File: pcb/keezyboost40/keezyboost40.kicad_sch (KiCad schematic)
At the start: 89 parts, among them SW1 SW_SPST, SW10 SW_SPST, SW11 SW_SPST, SW12 SW_SPST, SW13 SW_SPST, SW14 SW_SPST, SW15 SW_SPST, SW16 SW_SPST, SW17 SW_SPST, SW18 SW_SPST, SW19 SW_SPST, SW2 SW_SPST, SW20 SW_SPST, SW21 SW_SPST, SW22 SW_SPST, SW23 SW_SPST, SW24 SW_SPST, SW25 SW_SPST, SW26 SW_SPST, SW27 SW_SPST, SW28 SW_SPST, SW29 SW_SPST, SW3 SW_SPST, SW30 SW_SPST, SW31 SW_SPST, SW32 SW_SPST, SW33 SW_SPST, SW34 SW_SPST, SW35 SW_SPST, SW36 SW_SPST, SW37 SW_SPST, SW38 SW_SPST, SW39 SW_SPST, SW4 SW_SPST, SW40 SW_SPST, SW5 SW_SPST, SW6 SW_SPST, SW7 SW_SPST, SW8 SW_SPST, SW9 SW_SPST, U1 Pico, U2 ST7735_1.8inch

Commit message: finish v0.0
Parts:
- removed BZ1: Buzzer, symbol Device:Buzzer
- removed JP1: SolderJumper_2_Open, symbol Jumper:SolderJumper_2_Open
- removed JP2: (no value), symbol Jumper:SolderJumper_2_Open
- removed R1: R, symbol Device:R
- removed R2: (no value), symbol Device:R
- removed RV1: R_Potentiometer_Trim, symbol Device:R_Potentiometer_Trim
- removed RV2: (no value), symbol Device:R_Potentiometer_Trim
- added H1, H5: (no value), symbol Mechanical:MountingHole
- added H10, H2, H3, H4, H6, H7, H8, H9: MountingHole, symbol Mechanical:MountingHole
- U1: footprint RPi_Pico:RPi_Pico_SMD_TH -> (none)
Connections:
- net 3v3: now also U2.1 (VCC)

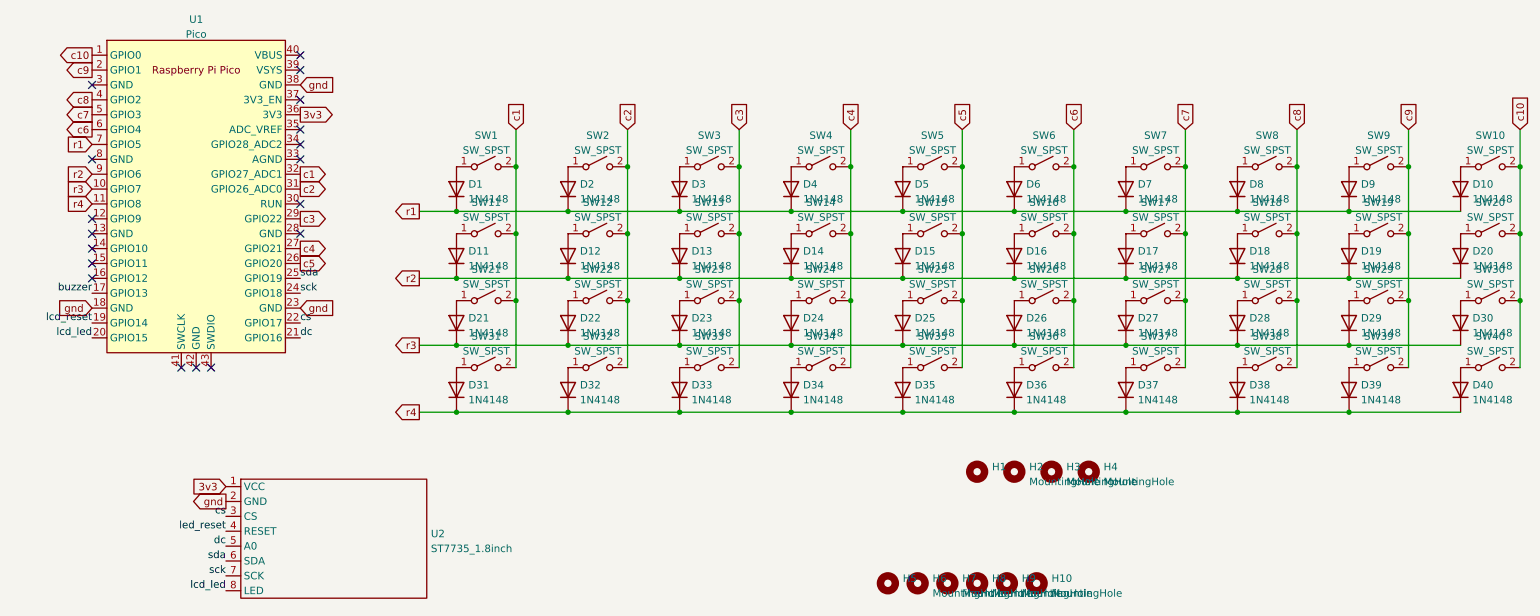
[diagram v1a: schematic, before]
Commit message: fixup issues with lcd interface connections
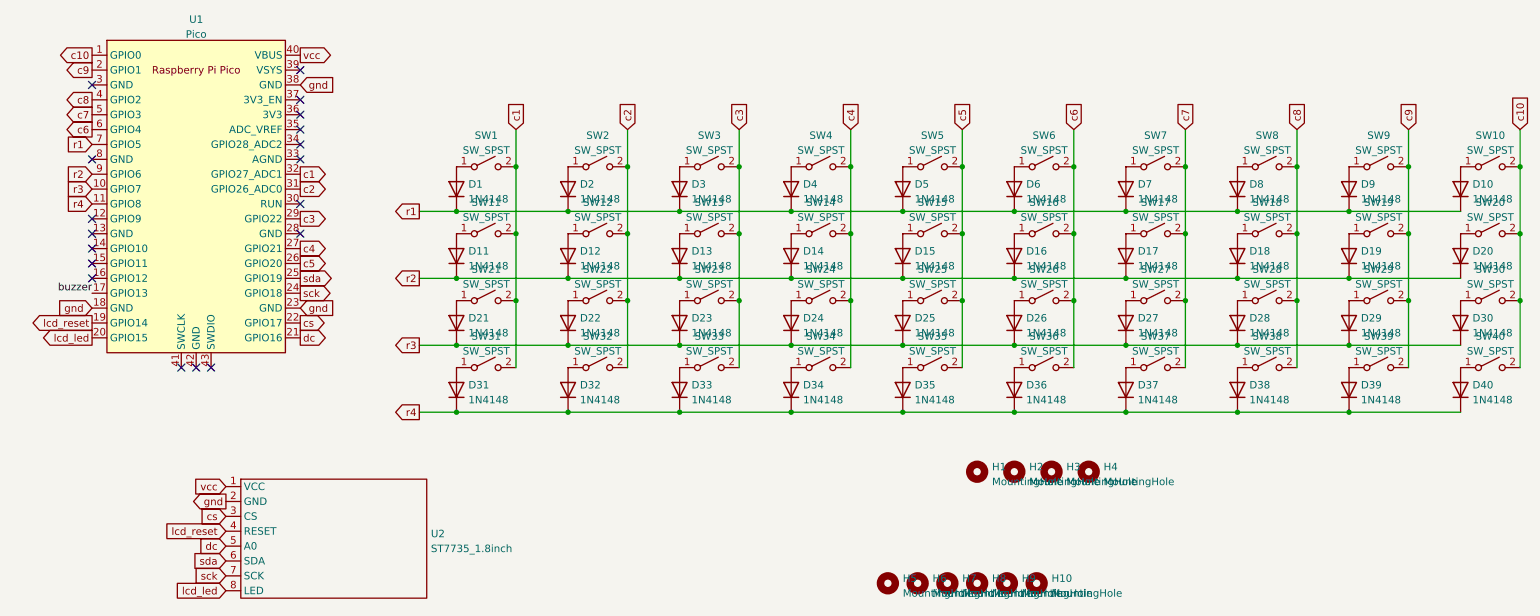
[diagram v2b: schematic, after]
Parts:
- D1, D10, D11, D12, D13, D14, D15, D16, D17, D18, D19, D2, D20, D21, D22, D23, D24, D25, D26, D27, D28, D29, D3, D30, D31, D32, D33, D34, D35, D36, D37, D38, D39, D4, D40, D5, D6, D7, D8, D9: footprint (none) -> Diode_SMD:D_SOD-123
- H1: value (none) -> MountingHole; footprint (none) -> MountingHole:MountingHole_2.2mm_M2_DIN965_Pad
- H10, H6, H7, H8, H9: footprint (none) -> MountingHole:MountingHole_2.2mm_M2
- H2, H3, H4: footprint (none) -> MountingHole:MountingHole_2.2mm_M2_DIN965_Pad
- H5: value (none) -> MountingHole; footprint (none) -> MountingHole:MountingHole_2.2mm_M2
- SW1, SW10, SW11, SW12, SW13, SW14, SW15, SW16, SW17, SW18, SW19, SW2, SW20, SW21, SW22, SW23, SW24, SW25, SW26, SW27, SW28, SW29, SW3, SW30, SW31, SW32, SW33, SW34, SW35, SW36, SW37, SW38, SW39, SW4, SW40, SW5, SW6, SW7, SW8, SW9: footprint (none) -> keyswitches:Kailh_socket_PG1350
- U1: footprint (none) -> kicub_keyboard_extras:RPi_Pico_SMD_TH_OPEN
- U2: footprint (none) -> kicub_keyboard_extras:ST7735_1.8inch
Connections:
- net led_reset is gone; now on net lcd_reset: U2.4 (RESET)
- net vcc: now reaches U1.40 (VBUS)
- net vcc: now also U2.1 (VCC)
- net 3v3: no longer names the net of U1.36 (3V3)
- net 3v3: no longer U2.1 (VCC)

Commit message: make lcd use 3.3v over 5v
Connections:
- net vcc: now also U1.36 (3V3); no longer U1.40 (VBUS)
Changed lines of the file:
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@@
   (no_connect (at 26.67 60.96))
   (no_connect (at 26.67 50.8))
+  (no_connect (at 62.23 33.02))
   (no_connect (at 62.23 40.64))
   (no_connect (at 62.23 35.56))
@@
   (no_connect (at 44.45 86.36))
   (no_connect (at 46.99 86.36))
-  (no_connect (at 62.23 43.18))
   (wire (pts (xy 137.16 74.93) (xy 137.16 86.36))
     (stroke (width 0) (type default) (color 0 0 0 0))
@@
     )
   )
+  (global_label "vcc" (shape output) (at 62.23 43.18 0) (fields_autoplaced)
+    (effects (font (size 1.27 1.27)) (justify left))
+    (property "Intersheet References" "${INTERSHEET_REFS}" (id 0) (at 67.7879 43.1006 0)
+      (effects (font (size 1.27 1.27)) (justify left) hide)
+    )
+  )
   (global_label "sck" (shape output) (at 62.23 73.66 0) (fields_autoplaced)
     (effects (font (size 1.27 1.27)) (justify left))
@@
     )
   )
-  (global_label "vcc" (shape output) (at 62.23 33.02 0) (fields_autoplaced)
-    (effects (font (size 1.27 1.27)) (justify left))
-    (property "Intersheet References" "${INTERSHEET_REFS}" (id 0) (at 67.7879 32.9406 0)
-      (effects (font (size 1.27 1.27)) (justify left) hide)
-    )
-  )

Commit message: add reset button
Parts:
- added SW41: (no value), symbol Switch:SW_SPST
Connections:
- net gnd: now also SW41.1 (A)
- net buzzer: no longer names the net of U1.17 (GPIO13)
- net buzzer: now also SW41.2 (B)
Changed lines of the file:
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@@
 (kicad_sch (version 20211123) (generator eeschema)
   (paper "A4")
+  (junction (at 21.59 76.2) (diameter 0) (color 0 0 0 0)
+  )
   (junction (at 222.25 93.98) (diameter 0) (color 0 0 0 0)
   )
@@
     (stroke (width 0) (type default) (color 0 0 0 0))
   )
+  (wire (pts (xy 20.32 76.2) (xy 21.59 76.2))
+    (stroke (width 0) (type default) (color 0 0 0 0))
+  )
   (wire (pts (xy 203.2 71.12) (xy 222.25 71.12))
     (stroke (width 0) (type default) (color 0 0 0 0))
@@
     (stroke (width 0) (type default) (color 0 0 0 0))
   )
+  (wire (pts (xy 21.59 73.66) (xy 21.59 76.2))
+    (stroke (width 0) (type default) (color 0 0 0 0))
+  )
   (wire (pts (xy 175.26 52.07) (xy 175.26 63.5))
     (stroke (width 0) (type default) (color 0 0 0 0))
@@
     (stroke (width 0) (type default) (color 0 0 0 0))
   )
+  (wire (pts (xy 16.51 73.66) (xy 21.59 73.66))
+    (stroke (width 0) (type default) (color 0 0 0 0))
+  )
   (wire (pts (xy 194.31 45.72) (xy 194.31 52.07))
     (stroke (width 0) (type default) (color 0 0 0 0))
@@
     (stroke (width 0) (type default) (color 0 0 0 0))
   )
+  (wire (pts (xy 21.59 76.2) (xy 26.67 76.2))
+    (stroke (width 0) (type default) (color 0 0 0 0))
+  )
   (wire (pts (xy 165.1 93.98) (xy 184.15 93.98))
     (stroke (width 0) (type default) (color 0 0 0 0))
@@
   (wire (pts (xy 156.21 63.5) (xy 156.21 74.93))
     (stroke (width 0) (type default) (color 0 0 0 0))
-  )
-  (label "buzzer" (at 26.67 73.66 180)
-    (effects (font (size 1.27 1.27)) (justify right bottom))
   )
   (global_label "cs" (shape output) (at 62.23 78.74 0) (fields_autoplaced)
@@
     )
   )
-  (global_label "gnd" (shape input) (at 26.67 76.2 180) (fields_autoplaced)
+  (global_label "gnd" (shape input) (at 20.32 76.2 180) (fields_autoplaced)
     (effects (font (size 1.27 1.27)) (justify right))
-    (property "Intersheet References" "${INTERSHEET_REFS}" (id 0) (at 20.8098 76.1206 0)
+    (property "Intersheet References" "${INTERSHEET_REFS}" (id 0) (at 14.4598 76.1206 0)
       (effects (font (size 1.27 1.27)) (justify right) hide)
     )
@@
     (pin "2")
   )
+  (symbol (lib_id "Switch:SW_SPST") (at 21.59 73.66 0) (unit 1)
+    (in_bom yes) (on_board yes) (fields_autoplaced)
+    (property "Reference" "SW41" (id 0) (at 21.59 68.3092 0))
+    (property "Value" "" (id 1) (at 21.59 70.8461 0))
+    (property "Footprint" "" (id 2) (at 21.59 73.66 0)
+      (effects (font (size 1.27 1.27)) hide)
+    )
+    (property "Datasheet" "~" (id 3) (at 21.59 73.66 0)
+      (effects (font (size 1.27 1.27)) hide)
+    )
+    (pin "1")
+    (pin "2")
+  )
   (symbol (lib_id "Switch:SW_SPST") (at 246.38 86.36 0) (unit 1)
     (in_bom yes) (on_board yes) (fields_autoplaced)
@@
       (reference "SW40") (unit 1) (value "SW_SPST") (footprint "keyswitches:Kailh_socket_PG1350")
     )
+    (path "/f2cea19d-f80c-460b-b19f-cd2ae20ae1b0"
+      (reference "SW41") (unit 1) (value "SW_SPST") (footprint "Button_Switch_SMD:SW_SPST_FSMSM")
+    )
     (path "/8f01bcf5-6c5d-49f8-bd12-9b8c6985e760"
